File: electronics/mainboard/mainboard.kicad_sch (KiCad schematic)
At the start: 25 parts, among them Q1 TSM250N02CX_RFG, Q2 TSM250N02CX_RFG, SW1 SW_Push, SW10 SW_Push, SW11 SW_Push, SW12 SW_Push, SW13 SW_Push, SW14 SW_Push, SW15 SW_Push, SW2 SW_Push, SW3 SW_Push, SW4 SW_Push, SW5 SW_Push, SW6 SW_Push, SW7 SW_Push, SW8 SW_Push, SW9 SW_Push, U1 1022

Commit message: modified
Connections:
- net at A1.26 (A7): no longer Q2.1
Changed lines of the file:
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@@
-    (stroke (width 0) (type default) (color 0 0 0 0))
-  )
-  (wire (pts (xy 234.95 111.76) (xy 251.46 111.76))
     (stroke (width 0) (type default) (color 0 0 0 0))
   )

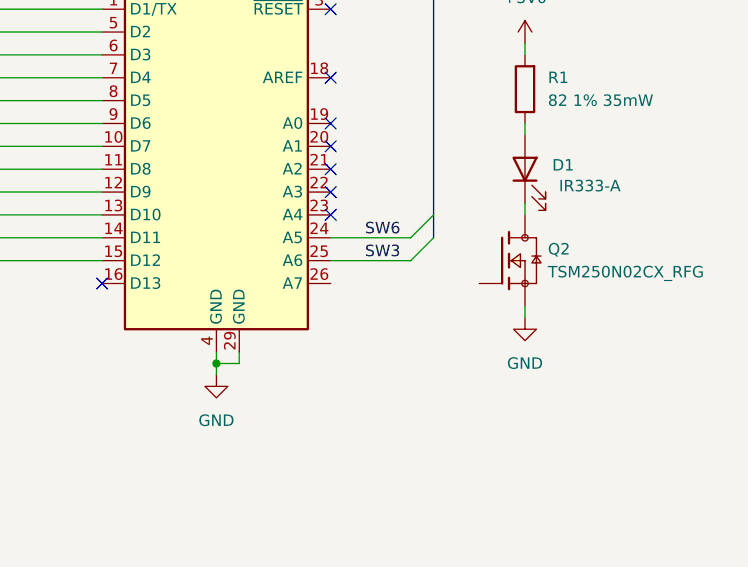
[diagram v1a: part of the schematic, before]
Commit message: correct DRC error
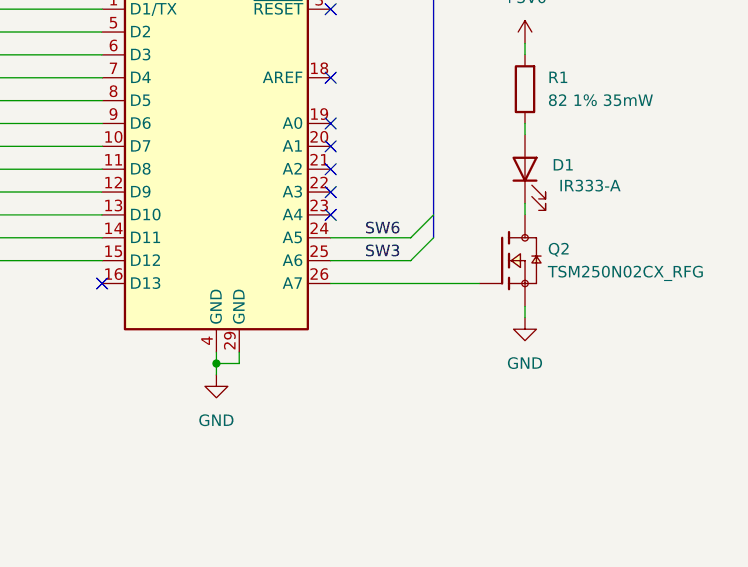
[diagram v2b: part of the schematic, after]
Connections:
- net at A1.26 (A7): now also Q2.1
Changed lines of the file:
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@@
+    (stroke (width 0) (type default) (color 0 0 0 0))
+  )
+  (wire (pts (xy 234.95 111.76) (xy 251.46 111.76))
     (stroke (width 0) (type default) (color 0 0 0 0))
   )

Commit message: some changes
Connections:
- net at A1.26 (A7): no longer Q2.1
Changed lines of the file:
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@@
-    (stroke (width 0) (type default) (color 0 0 0 0))
-  )
-  (wire (pts (xy 234.95 111.76) (xy 251.46 111.76))
     (stroke (width 0) (type default) (color 0 0 0 0))
   )

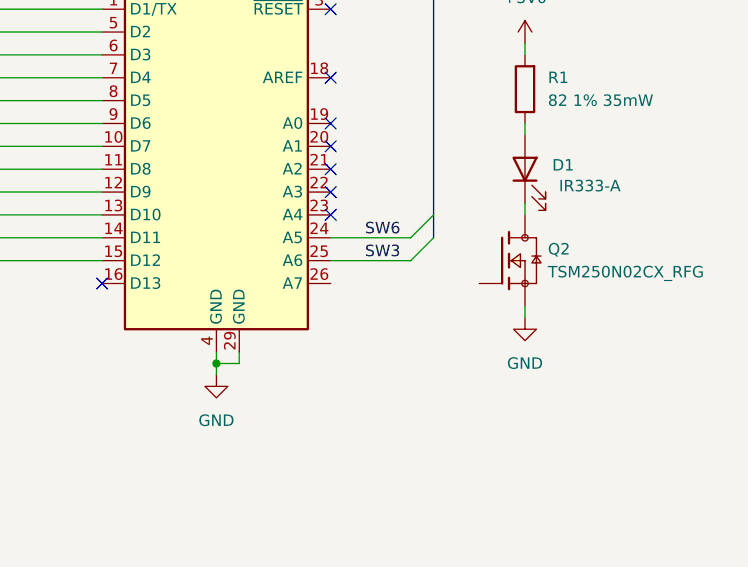
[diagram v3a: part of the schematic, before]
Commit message: correct missing line
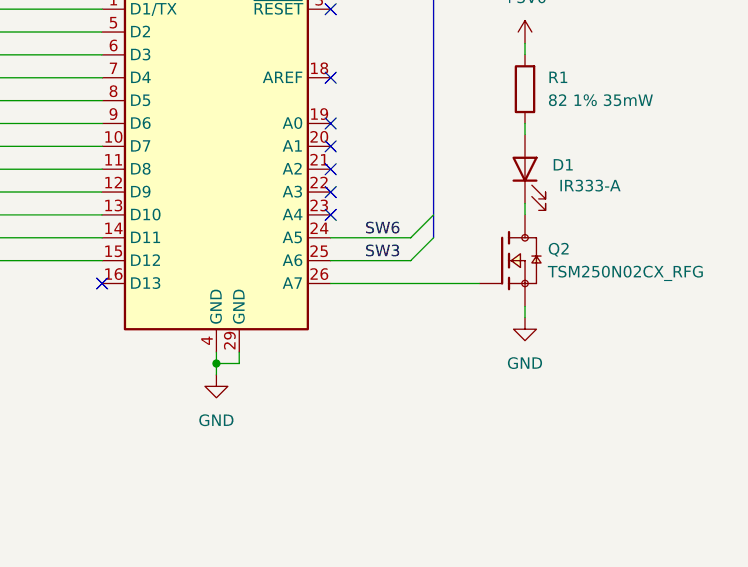
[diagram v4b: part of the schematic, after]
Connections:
- net at A1.26 (A7): now also Q2.1
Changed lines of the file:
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@@
+    (stroke (width 0) (type default) (color 0 0 0 0))
+  )
+  (wire (pts (xy 234.95 111.76) (xy 251.46 111.76))
     (stroke (width 0) (type default) (color 0 0 0 0))
   )

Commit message: some modifictions
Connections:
- net at A1.26 (A7): no longer Q2.1
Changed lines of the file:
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@@
-    (stroke (width 0) (type default) (color 0 0 0 0))
-  )
-  (wire (pts (xy 234.95 111.76) (xy 251.46 111.76))
     (stroke (width 0) (type default) (color 0 0 0 0))
   )

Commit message: bugfix
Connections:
- net at A1.26 (A7): now also Q2.1
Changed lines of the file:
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@@
+    (stroke (width 0) (type default) (color 0 0 0 0))
+  )
+  (wire (pts (xy 234.95 111.76) (xy 251.46 111.76))
     (stroke (width 0) (type default) (color 0 0 0 0))
   )
